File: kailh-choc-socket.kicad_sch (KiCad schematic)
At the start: 8 parts, among them SW1 SW_DIP_x01

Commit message: Added layer details
M  .gitignore
M  README.md
M  fp-lib-table
M  kailh-choc-socket.kicad_pcb
M  kailh-choc-socket.kicad_prl
M  kailh-choc-socket.kicad_pro
M  kailh-choc-socket.kicad_sch
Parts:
- removed H1, H6: MountingHole_Pad, MountingHole:MountingHole_2.2mm_M2_Pad_Via, symbol Mechanical:MountingHole_Pad
- removed H2, H3, H4, H5: MountingHole, MountingHole:MountingHole_2mm, symbol Mechanical:MountingHole
- removed SW1: SW_DIP_x01, Switch_Keyboard_Hotswap_Kailh:SW_Hotswap_Kailh_Choc_V1_1.00u, symbol Switch:SW_DIP_x01
- added J1, J2, J3, J4, J5, J6, J7, J8: Conn_01x01_Male, Giri-Kailh-Choc-Library:TestPoint_THTPad_1.0x1.5mm_Drill0.5mm, symbol Connector:Conn_01x01_Male
- added SW1: SW_DIP_x02, Giri-Kailh-Choc-Library:SW_Hotswap_Kailh_Choc_V1_plated_girish2, symbol Switch:SW_DIP_x02
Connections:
- net at D1.2 (A): now also J4.1 (Pin_1), J5.1 (Pin_1)
- net at D1.1 (K): now also SW1.1
- new net: J2.1 (Pin_1), J8.1 (Pin_1), SW1.4
- new net: J3.1 (Pin_1), J6.1 (Pin_1), SW1.3
- new net: J1.1 (Pin_1), J7.1 (Pin_1), SW1.2
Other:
- moved on the sheet: D1

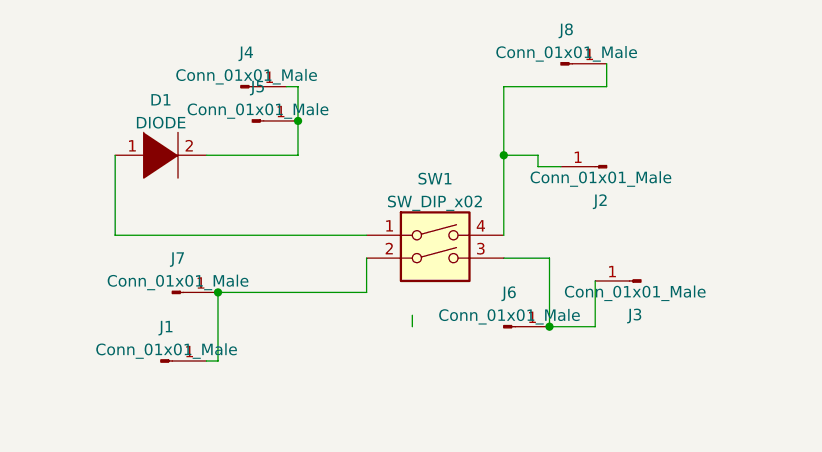
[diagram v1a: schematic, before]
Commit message: Add new footprints for mounting holes
A  Giri-Kailh-Choc-Library.pretty/D_SOD-123.kicad_mod
A  Giri-Kailh-Choc-Library.pretty/MountingHole_1.2mm_M1.kicad_mod
D  Giri-Kailh-Choc-Library.pretty/SW_Hotswap_Kailh_Choc_V1_plated_girish.kicad_mod
M  Giri-Kailh-Choc-Library.pretty/SW_Hotswap_Kailh_Choc_V1_plated_girish2.kicad_mod
M  Giri-Kailh-Choc-Library.pretty/TestPoint_THTPad_1.0x1.5mm_Drill0.5mm.kicad_mod
A  Giri-Kailh-Choc-Library.pretty/TestPoint_THTPad_1.0x2.5mm_Drill0.5mm.kicad_mod
M  kailh-choc-socket.kicad_pcb
M  kailh-choc-socket.kicad_prl
M  kailh-choc-socket.kicad_sch
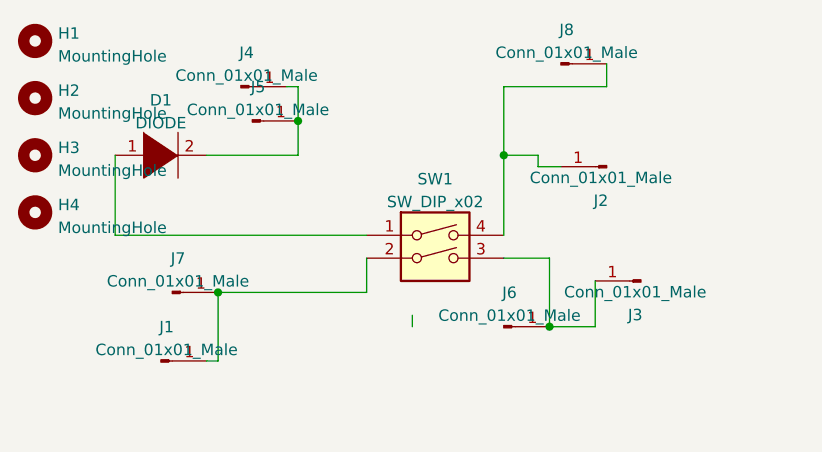
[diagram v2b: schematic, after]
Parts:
- added H1, H2, H3, H4: MountingHole, Giri-Kailh-Choc-Library:MountingHole_1.2mm_M1, symbol Mechanical:MountingHole
- D1: footprint Diode_SMD:D_SOD-123 -> Giri-Kailh-Choc-Library:D_SOD-123
- J1, J2, J4, J5, J6, J7, J8: footprint Giri-Kailh-Choc-Library:TestPoint_THTPad_1.0x1.5mm_Drill0.5mm -> Giri-Kailh-Choc-Library:TestPoint_THTPad_1.0x2.5mm_Drill0.5mm
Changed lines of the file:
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@@
     (stroke (width 0) (type default) (color 0 0 0 0))
+  )
+  (symbol (lib_id "Mechanical:MountingHole") (at 104.14 52.07 0) (unit 1)
+    (in_bom yes) (on_board yes) (fields_autoplaced)
+    (property "Reference" "H2" (id 0) (at 106.68 51.2353 0)
+      (effects (font (size 1.27 1.27)) (justify left))
+    )
+    (property "Value" "MountingHole" (id 1) (at 106.68 53.7722 0)
+      (effects (font (size 1.27 1.27)) (justify left))
+    )
+    (property "Footprint" "Giri-Kailh-Choc-Library:MountingHole_1.2mm_M1" (id 2) (at 104.14 52.07 0)
+      (effects (font (size 1.27 1.27)) hide)
+    )
+    (property "Datasheet" "~" (id 3) (at 104.14 52.07 0)
+      (effects (font (size 1.27 1.27)) hide)
+    )
   )
   (symbol (lib_id "Connector:Conn_01x01_Male") (at 162.56 48.26 0) (unit 1)
@@
     (property "Reference" "J8" (id 0) (at 163.195 44.484 0))
     (property "Value" "Conn_01x01_Male" (id 1) (at 163.195 47.0209 0))
-    (property "Footprint" "Giri-Kailh-Choc-Library:TestPoint_THTPad_1.0x1.5mm_Drill0.5mm" (id 2) (at 162.56 48.26 0)
+    (property "Footprint" "Giri-Kailh-Choc-Library:TestPoint_THTPad_1.0x2.5mm_Drill0.5mm" (id 2) (at 162.56 48.26 0)
       (effects (font (size 1.27 1.27)) hide)
     )
@@
     (property "Reference" "J6" (id 0) (at 156.845 73.694 0))
     (property "Value" "Conn_01x01_Male" (id 1) (at 156.845 76.2309 0))
-    (property "Footprint" "Giri-Kailh-Choc-Library:TestPoint_THTPad_1.0x1.5mm_Drill0.5mm" (id 2) (at 156.21 77.47 0)
+    (property "Footprint" "Giri-Kailh-Choc-Library:TestPoint_THTPad_1.0x2.5mm_Drill0.5mm" (id 2) (at 156.21 77.47 0)
       (effects (font (size 1.27 1.27)) hide)
     )
@@
     (property "Reference" "J2" (id 0) (at 167.005 63.466 0))
     (property "Value" "Conn_01x01_Male" (id 1) (at 167.005 60.9291 0))
-    (property "Footprint" "Giri-Kailh-Choc-Library:TestPoint_THTPad_1.0x1.5mm_Drill0.5mm" (id 2) (at 167.64 59.69 0)
+    (property "Footprint" "Giri-Kailh-Choc-Library:TestPoint_THTPad_1.0x2.5mm_Drill0.5mm" (id 2) (at 167.64 59.69 0)
       (effects (font (size 1.27 1.27)) hide)
     )
@@
     )
     (pin "1")
+  )
+  (symbol (lib_id "Mechanical:MountingHole") (at 104.14 45.72 0) (unit 1)
+    (in_bom yes) (on_board yes) (fields_autoplaced)
+    (property "Reference" "H1" (id 0) (at 106.68 44.8853 0)
+      (effects (font (size 1.27 1.27)) (justify left))
+    )
+    (property "Value" "MountingHole" (id 1) (at 106.68 47.4222 0)
+      (effects (font (size 1.27 1.27)) (justify left))
+    )
+    (property "Footprint" "Giri-Kailh-Choc-Library:MountingHole_1.2mm_M1" (id 2) (at 104.14 45.72 0)
+      (effects (font (size 1.27 1.27)) hide)
+    )
+    (property "Datasheet" "~" (id 3) (at 104.14 45.72 0)
+      (effects (font (size 1.27 1.27)) hide)
+    )
+  )
+  (symbol (lib_id "Mechanical:MountingHole") (at 104.14 58.42 0) (unit 1)
+    (in_bom yes) (on_board yes) (fields_autoplaced)
+    (property "Reference" "H3" (id 0) (at 106.68 57.5853 0)
+      (effects (font (size 1.27 1.27)) (justify left))
+    )
+    (property "Value" "MountingHole" (id 1) (at 106.68 60.1222 0)
+      (effects (font (size 1.27 1.27)) (justify left))
+    )
+    (property "Footprint" "Giri-Kailh-Choc-Library:MountingHole_1.2mm_M1" (id 2) (at 104.14 58.42 0)
+      (effects (font (size 1.27 1.27)) hide)
+    )
+    (property "Datasheet" "~" (id 3) (at 104.14 58.42 0)
+      (effects (font (size 1.27 1.27)) hide)
+    )
   )
   (symbol (lib_id "pspice:DIODE") (at 118.11 58.42 0) (unit 1)
@@
     (property "Reference" "D1" (id 0) (at 118.11 52.3072 0))
     (property "Value" "DIODE" (id 1) (at 118.11 54.8441 0))
-    (property "Footprint" "Diode_SMD:D_SOD-123" (id 2) (at 118.11 58.42 0)
+    (property "Footprint" "Giri-Kailh-Choc-Library:D_SOD-123" (id 2) (at 118.11 58.42 0)
       (effects (font (size 1.27 1.27)) hide)
     )
@@
     (property "Reference" "J1" (id 0) (at 118.745 77.504 0))
     (property "Value" "Conn_01x01_Male" (id 1) (at 118.745 80.0409 0))
-    (property "Footprint" "Giri-Kailh-Choc-Library:TestPoint_THTPad_1.0x1.5mm_Drill0.5mm" (id 2) (at 118.11 81.28 0)
+    (property "Footprint" "Giri-Kailh-Choc-Library:TestPoint_THTPad_1.0x2.5mm_Drill0.5mm" (id 2) (at 118.11 81.28 0)
       (effects (font (size 1.27 1.27)) hide)
     )
@@
     )
     (pin "1")
+  )
+  (symbol (lib_id "Mechanical:MountingHole") (at 104.14 64.77 0) (unit 1)
+    (in_bom yes) (on_board yes) (fields_autoplaced)
+    (property "Reference" "H4" (id 0) (at 106.68 63.9353 0)
+      (effects (font (size 1.27 1.27)) (justify left))
+    )
+    (property "Value" "MountingHole" (id 1) (at 106.68 66.4722 0)
+      (effects (font (size 1.27 1.27)) (justify left))
+    )
+    (property "Footprint" "Giri-Kailh-Choc-Library:MountingHole_1.2mm_M1" (id 2) (at 104.14 64.77 0)
+      (effects (font (size 1.27 1.27)) hide)
+    )
+    (property "Datasheet" "~" (id 3) (at 104.14 64.77 0)
+      (effects (font (size 1.27 1.27)) hide)
+    )
   )
   (symbol (lib_id "Connector:Conn_01x01_Male") (at 119.38 73.66 0) (unit 1)
@@
     (property "Reference" "J7" (id 0) (at 120.015 69.884 0))
     (property "Value" "Conn_01x01_Male" (id 1) (at 120.015 72.4209 0))
-    (property "Footprint" "Giri-Kailh-Choc-Library:TestPoint_THTPad_1.0x1.5mm_Drill0.5mm" (id 2) (at 119.38 73.66 0)
+    (property "Footprint" "Giri-Kailh-Choc-Library:TestPoint_THTPad_1.0x2.5mm_Drill0.5mm" (id 2) (at 119.38 73.66 0)
       (effects (font (size 1.27 1.27)) hide)
     )
@@
     (property "Reference" "J4" (id 0) (at 127.635 47.024 0))
     (property "Value" "Conn_01x01_Male" (id 1) (at 127.635 49.5609 0))
-    (property "Footprint" "Giri-Kailh-Choc-Library:TestPoint_THTPad_1.0x1.5mm_Drill0.5mm" (id 2) (at 127 50.8 0)
+    (property "Footprint" "Giri-Kailh-Choc-Library:TestPoint_THTPad_1.0x2.5mm_Drill0.5mm" (id 2) (at 127 50.8 0)
       (effects (font (size 1.27 1.27)) hide)
     )
@@
     (property "Reference" "J5" (id 0) (at 128.905 50.834 0))
     (property "Value" "Conn_01x01_Male" (id 1) (at 128.905 53.3709 0))
-    (property "Footprint" "Giri-Kailh-Choc-Library:TestPoint_THTPad_1.0x1.5mm_Drill0.5mm" (id 2) (at 128.27 54.61 0)
+    (property "Footprint" "Giri-Kailh-Choc-Library:TestPoint_THTPad_1.0x2.5mm_Drill0.5mm" (id 2) (at 128.27 54.61 0)
       (effects (font (size 1.27 1.27)) hide)
     )
@@
   (symbol_instances
     (path "/a3e86e56-9deb-433f-ac4a-b3b6bb474e02"
-      (reference "D1") (unit 1) (value "DIODE") (footprint "Diode_SMD:D_SOD-123")
+      (reference "D1") (unit 1) (value "DIODE") (footprint "Giri-Kailh-Choc-Library:D_SOD-123")
+    )
+    (path "/683ec5d2-a1e2-4b7c-88ff-16e5543c82f6"
+      (reference "H1") (unit 1) (value "MountingHole") (footprint "Giri-Kailh-Choc-Library:MountingHole_1.2mm_M1")
+    )
+    (path "/0978854b-7f2d-4e70-81ad-b8366855ab91"
+      (reference "H2") (unit 1) (value "MountingHole") (footprint "Giri-Kailh-Choc-Library:MountingHole_1.2mm_M1")
+    )
+    (path "/8d14e609-ecde-4de8-9963-5f1ace4ff4c2"
+      (reference "H3") (unit 1) (value "MountingHole") (footprint "Giri-Kailh-Choc-Library:MountingHole_1.2mm_M1")
+    )
+    (path "/d1816e1a-9035-4e82-88a0-83bdc1c70357"
+      (reference "H4") (unit 1) (value "MountingHole") (footprint "Giri-Kailh-Choc-Library:MountingHole_1.2mm_M1")
     )
     (path "/cb6e11c9-9471-4a9b-9af5-208d08897519"
-      (reference "J1") (unit 1) (value "Conn_01x01_Male") (footprint "Giri-Kailh-Choc-Library:TestPoint_THTPad_1.0x1.5mm_Drill0.5mm")
+      (reference "J1") (unit 1) (value "Conn_01x01_Male") (footprint "Giri-Kailh-Choc-Library:TestPoint_THTPad_1.0x2.5mm_Drill0.5mm")
     )
     (path "/607dcc0b-586b-496b-9316-e34c8dbfe613"
-      (reference "J2") (unit 1) (value "Conn_01x01_Male") (footprint "Giri-Kailh-Choc-Library:TestPoint_THTPad_1.0x1.5mm_Drill0.5mm")
+      (reference "J2") (unit 1) (value "Conn_01x01_Male") (footprint "Giri-Kailh-Choc-Library:TestPoint_THTPad_1.0x2.5mm_Drill0.5mm")
     )
     (path "/fb141724-0ad2-4993-9639-eda2e17d8ee7"
@@
     )
     (path "/e8935454-8713-412e-89da-9e4c4b2e81bc"
-      (reference "J4") (unit 1) (value "Conn_01x01_Male") (footprint "Giri-Kailh-Choc-Library:TestPoint_THTPad_1.0x1.5mm_Drill0.5mm")
+      (reference "J4") (unit 1) (value "Conn_01x01_Male") (footprint "Giri-Kailh-Choc-Library:TestPoint_THTPad_1.0x2.5mm_Drill0.5mm")
     )
     (path "/f651eb1d-6032-4461-a4c6-b3851a4abb2c"
-      (reference "J5") (unit 1) (value "Conn_01x01_Male") (footprint "Giri-Kailh-Choc-Library:TestPoint_THTPad_1.0x1.5mm_Drill0.5mm")
+      (reference "J5") (unit 1) (value "Conn_01x01_Male") (footprint "Giri-Kailh-Choc-Library:TestPoint_THTPad_1.0x2.5mm_Drill0.5mm")
     )
     (path "/46cf0fa5-3358-4db9-ad78-e22dfb1c22ff"
-      (reference "J6") (unit 1) (value "Conn_01x01_Male") (footprint "Giri-Kailh-Choc-Library:TestPoint_THTPad_1.0x1.5mm_Drill0.5mm")
+      (reference "J6") (unit 1) (value "Conn_01x01_Male") (footprint "Giri-Kailh-Choc-Library:TestPoint_THTPad_1.0x2.5mm_Drill0.5mm")
     )
     (path "/d8bc2fe2-fba0-446d-a620-fb6b33636492"
-      (reference "J7") (unit 1) (value "Conn_01x01_Male") (footprint "Giri-Kailh-Choc-Library:TestPoint_THTPad_1.0x1.5mm_Drill0.5mm")
+      (reference "J7") (unit 1) (value "Conn_01x01_Male") (footprint "Giri-Kailh-Choc-Library:TestPoint_THTPad_1.0x2.5mm_Drill0.5mm")
     )
     (path "/181743ff-74dc-4f2c-91cb-dcb6366eea9e"
-      (reference "J8") (unit 1) (value "Conn_01x01_Male") (footprint "Giri-Kailh-Choc-Library:TestPoint_THTPad_1.0x1.5mm_Drill0.5mm")
+      (reference "J8") (unit 1) (value "Conn_01x01_Male") (footprint "Giri-Kailh-Choc-Library:TestPoint_THTPad_1.0x2.5mm_Drill0.5mm")
     )
     (path "/48d5e6f7-4e50-4e7d-8b77-2f6c2d801b60"
